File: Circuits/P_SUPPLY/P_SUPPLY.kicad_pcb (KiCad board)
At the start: 2 copper layers, 70.5 x 106.5 mm, 28 parts, among them P1 127VAC, P2 ON/OFF, P3 8V OUTPUT, P4 5V OUTPUT, T1 127:12, U1 LM7808CT, U2 LM7805CT, U3 LM7908CT

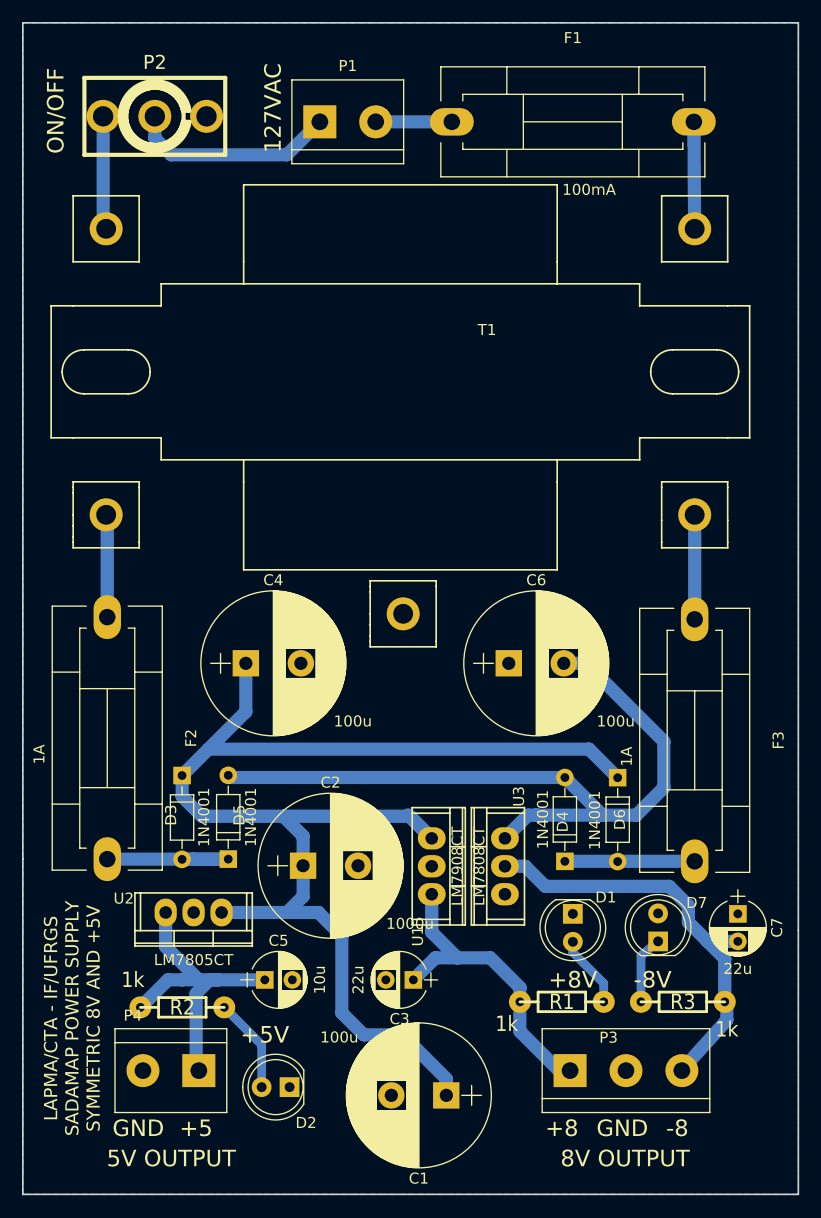
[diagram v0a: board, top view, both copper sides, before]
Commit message: ADD: Holes in Power Supply PCB
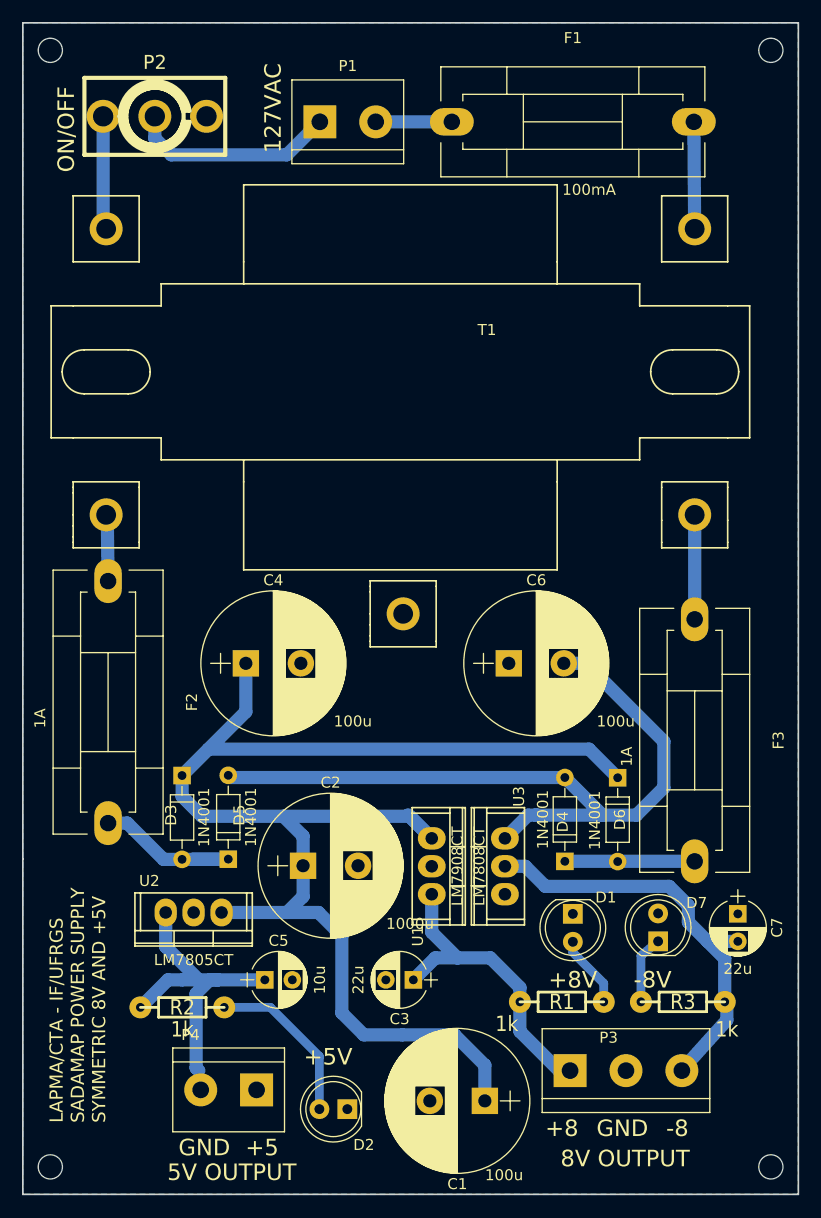
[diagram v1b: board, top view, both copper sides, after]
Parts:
- added REF**: MountingHole_2.2mm_M2, Mounting_Holes:MountingHole_2.2mm_M2, F.Cu at (101.0, 129.0)
- added REF**: MountingHole_2.2mm_M2, Mounting_Holes:MountingHole_2.2mm_M2, F.Cu at (35.5, 129.0)
- added REF**: MountingHole_2.2mm_M2, Mounting_Holes:MountingHole_2.2mm_M2, F.Cu at (35.5, 27.5)
- added REF**: MountingHole_2.2mm_M2, Mounting_Holes:MountingHole_2.2mm_M2, F.Cu at (101.0, 27.5)
- moved D2 5.62 mm to (62.5, 123.8)
- moved P4 5.53 mm to (54.2, 122.0)
- moved C1 3.54 mm to (75.0, 123.0)
- moved F2 3.28 mm to (40.8, 75.8)
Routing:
- net Net-(D2-Pad2): track 8.66 -> 15.3 mm
- net +12V: track 122.5 -> 127.2 mm
- net Net-(F2-Pad1): track 9.48 -> 6.21 mm

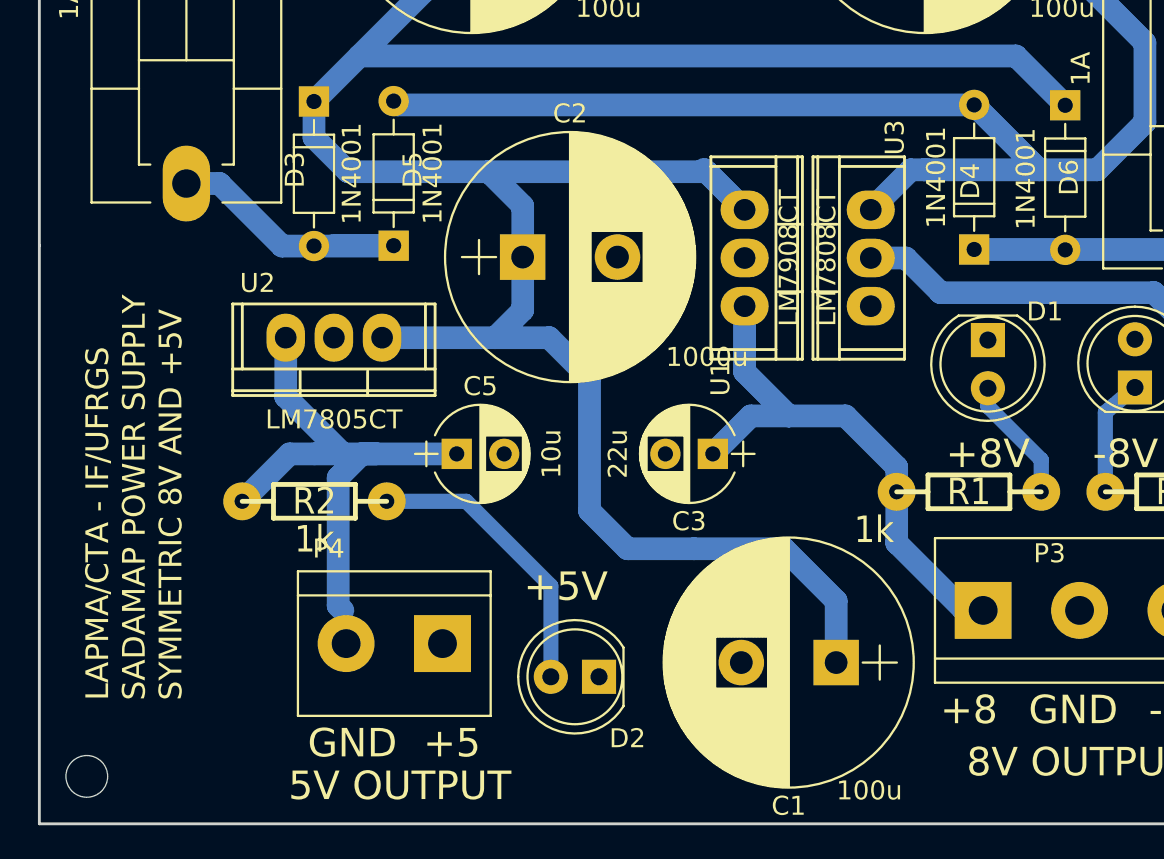
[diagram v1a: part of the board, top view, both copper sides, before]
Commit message: EDIT: Power Supply PCB Correction and ADD BOM
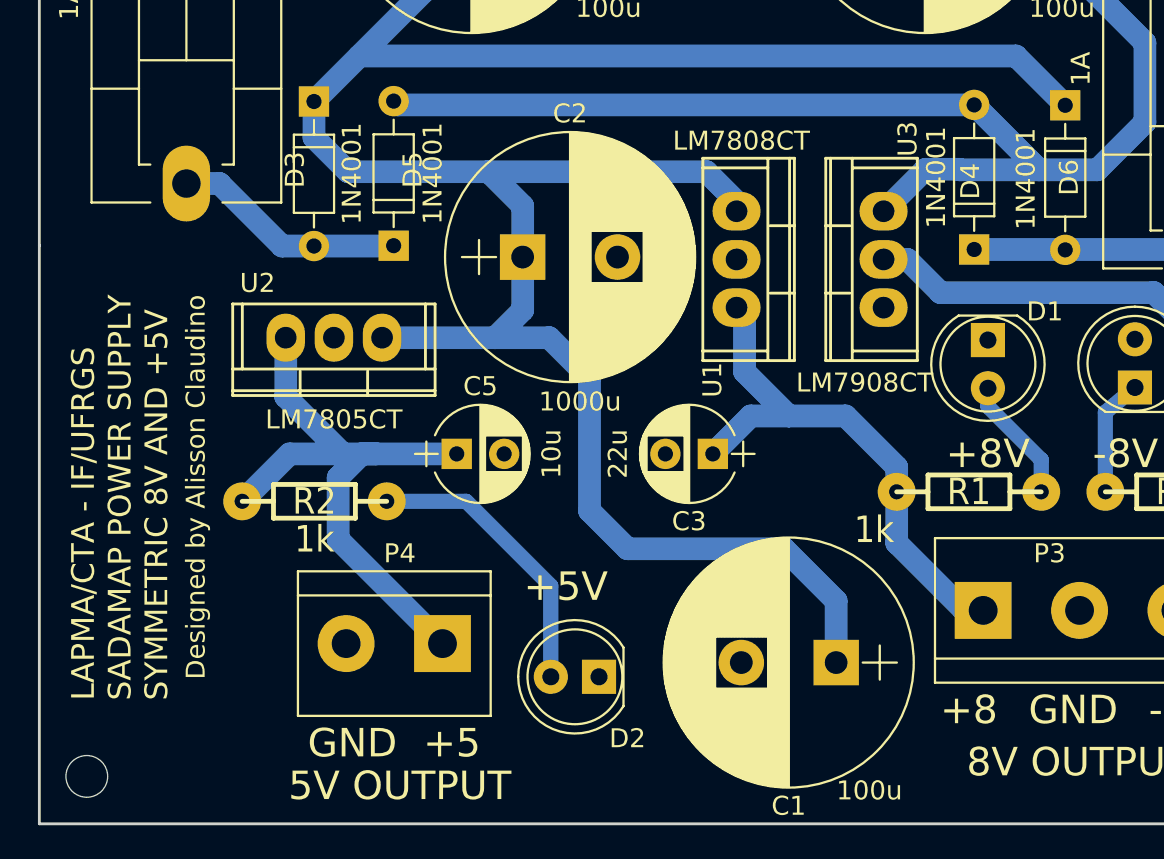
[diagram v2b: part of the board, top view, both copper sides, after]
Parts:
- moved U3 0.68 mm to (77.5, 101.8)
- moved U1 0.43 mm to (69.8, 101.8)
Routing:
- net +5V: track 29.3 -> 33.3 mm
- net Net-(D3-Pad1): track 15.5 -> 12.3 mm
- net +12V: track 127.2 -> 124.1 mm
- net -12V: track 68.3 -> 67.5 mm
- net -8V: track 39.6 -> 38.9 mm
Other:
- board text added: "Designed by Alisson Claudino"

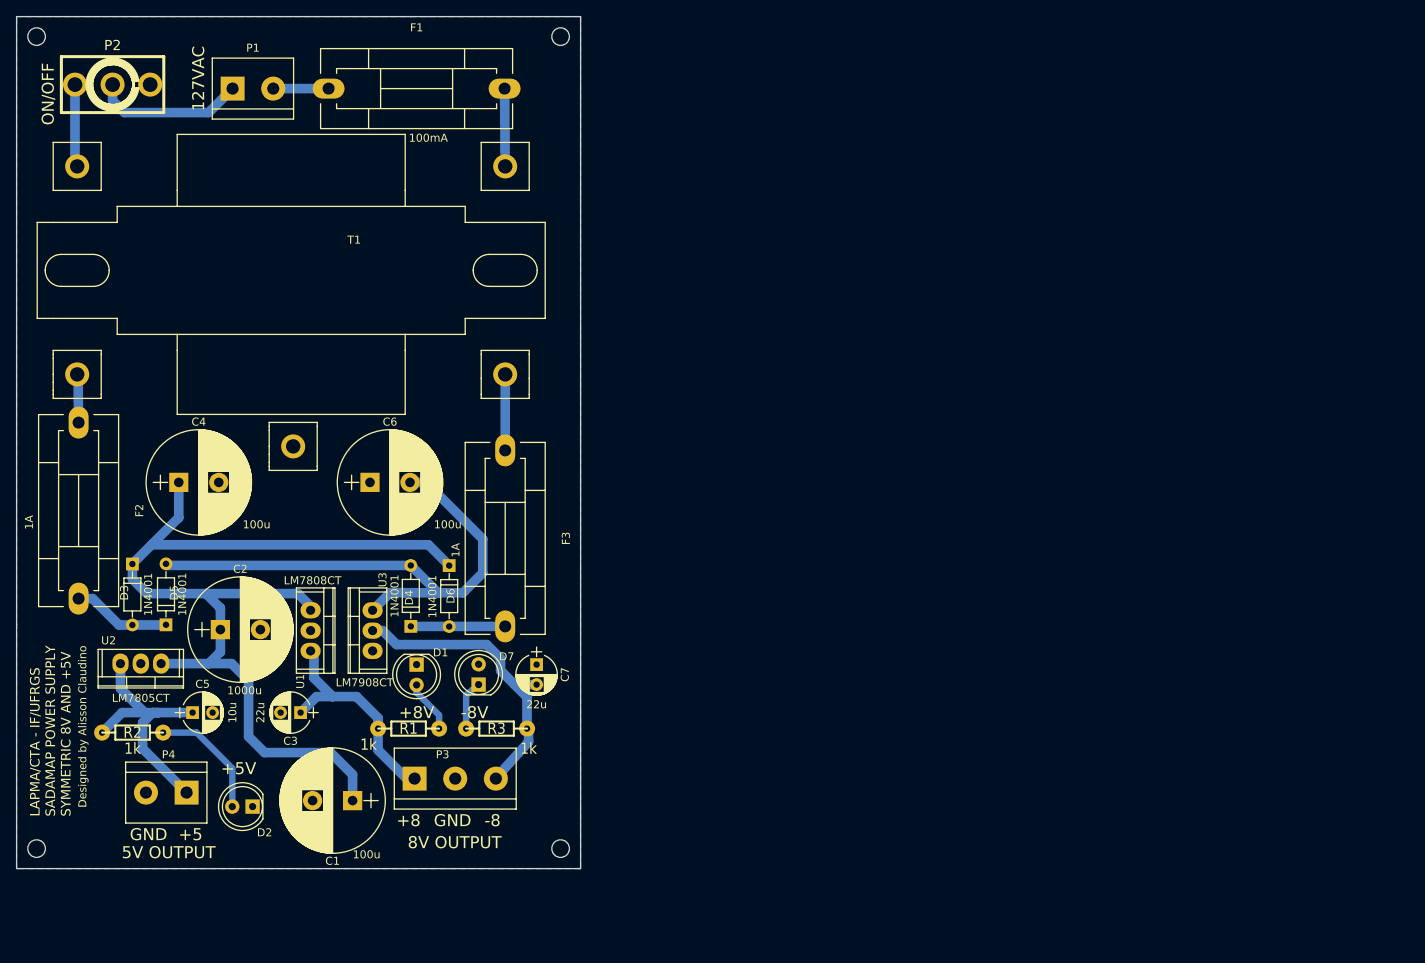
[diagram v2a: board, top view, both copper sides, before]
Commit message: ADD: Power Supply Fabrication Files
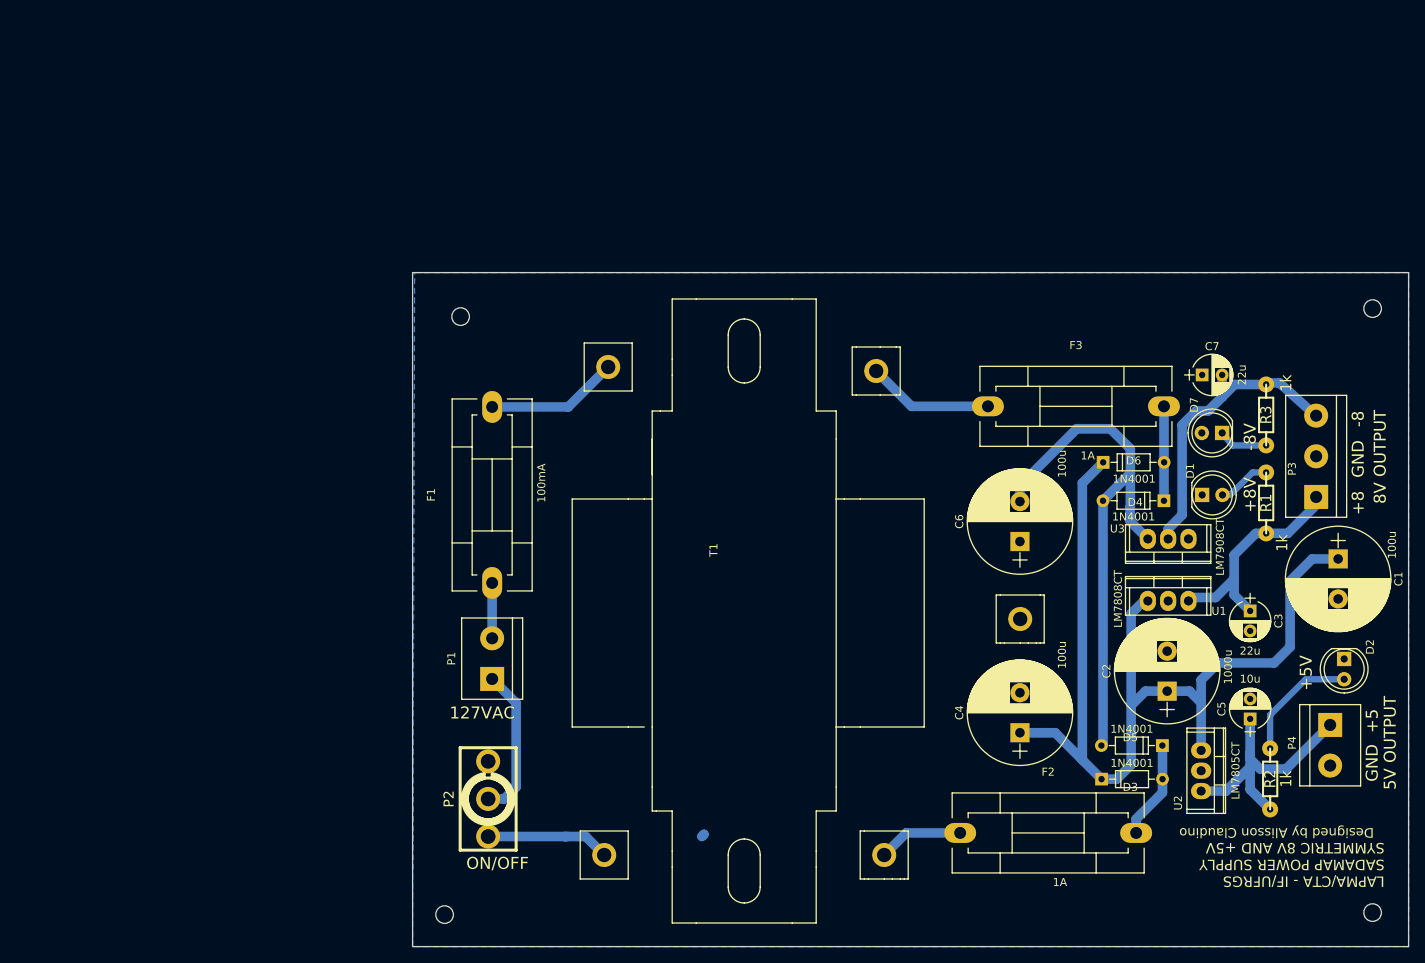
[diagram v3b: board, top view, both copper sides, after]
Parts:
- T1: footprint Transformers_THT:12V_transformer-3T -> Transformers_THT:12+12V_transformer_800mA-3T
- moved REF** 167.2 mm to (202.5, 137.0), turned to 90 degrees
- moved P4 143.2 mm to (197.2, 113.5), turned to 270 degrees
- moved R2 142.3 mm to (189.7, 120.3), turned to 90 degrees
- moved D2 137.7 mm to (198.9, 105.3), turned to 270 degrees
- moved U2 133.2 mm to (181.1, 119.3), turned to 270 degrees
- moved C5 132.2 mm to (187.2, 112.8), turned to 90 degrees
- moved C1 126.8 mm to (198.2, 92.8), turned to 270 degrees
- moved D3 125.5 mm to (176.2, 116.1), turned to 180 degrees
- moved D5 124.1 mm to (168.6, 120.3), turned to 0 degrees
- moved REF** 121.9 mm to (202.5, 61.5), turned to 90 degrees
- moved F2 121.5 mm to (150.9, 127.0), turned to 0 degrees
- moved REF** 121.0 mm to (86.5, 137.2), turned to 90 degrees
- moved C3 119.4 mm to (187.2, 99.3), turned to 270 degrees
- moved C2 118.6 mm to (176.8, 109.3), turned to 90 degrees
- moved P3 118.1 mm to (195.4, 85.0), turned to 90 degrees
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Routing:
- net Net-(F1-Pad2): track 9.73 -> 16.6 mm
- net Net-(F3-Pad1): track 9.50 -> 15.8 mm
- net Net-(P2-Pad1): track 10.9 -> 16.1 mm
- net Net-(F2-Pad1): track 6.21 -> 10.8 mm
- net (no net): track 0.00 -> 0.67 mm
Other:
- board size 70.5 x 106.5 mm -> 124.5 x 84.2 mm
